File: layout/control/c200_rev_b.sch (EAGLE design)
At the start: 66 parts, among them IC1 STM32F103C8T, IC2 LP2985-SOT23-5, IC3 IC_USBLC6-2, IC4 IC_USBLC6-2, IC5 LT1619ES8, IC6 LP2985-SOT23-5, IC7 IRF7470, T1 LPISR, X1 MINI-USB-SCHIELD-32005-201, Y1 532-CRYSTAL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

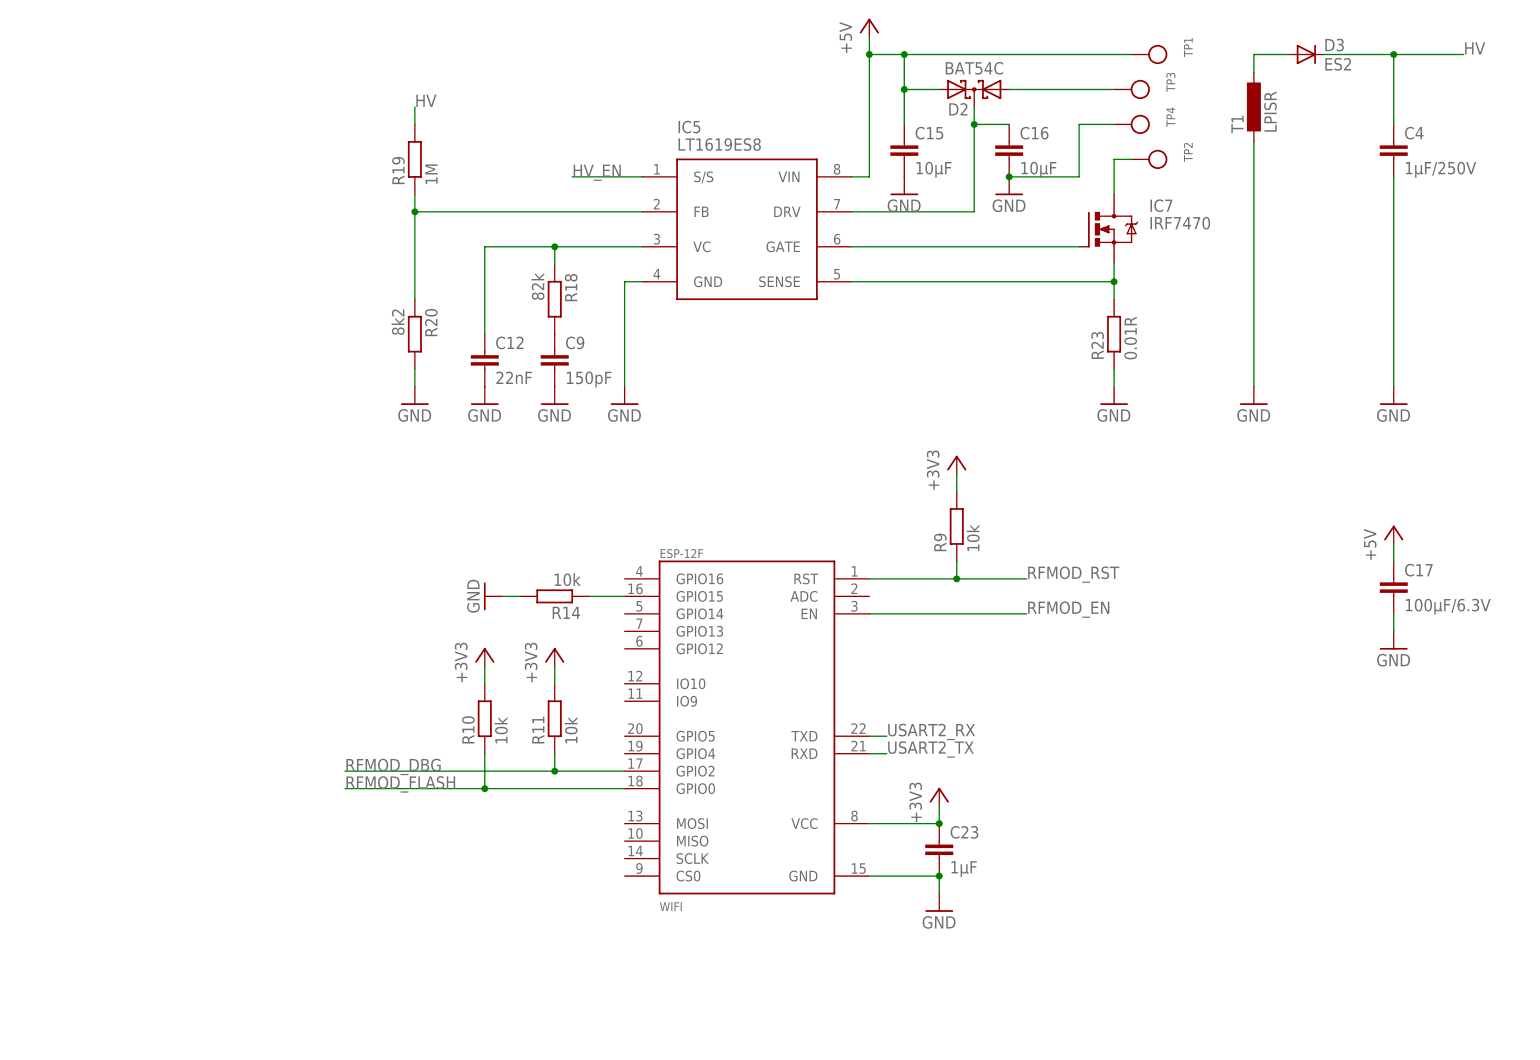
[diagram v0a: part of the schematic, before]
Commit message: Added rev. B of large clock layouts
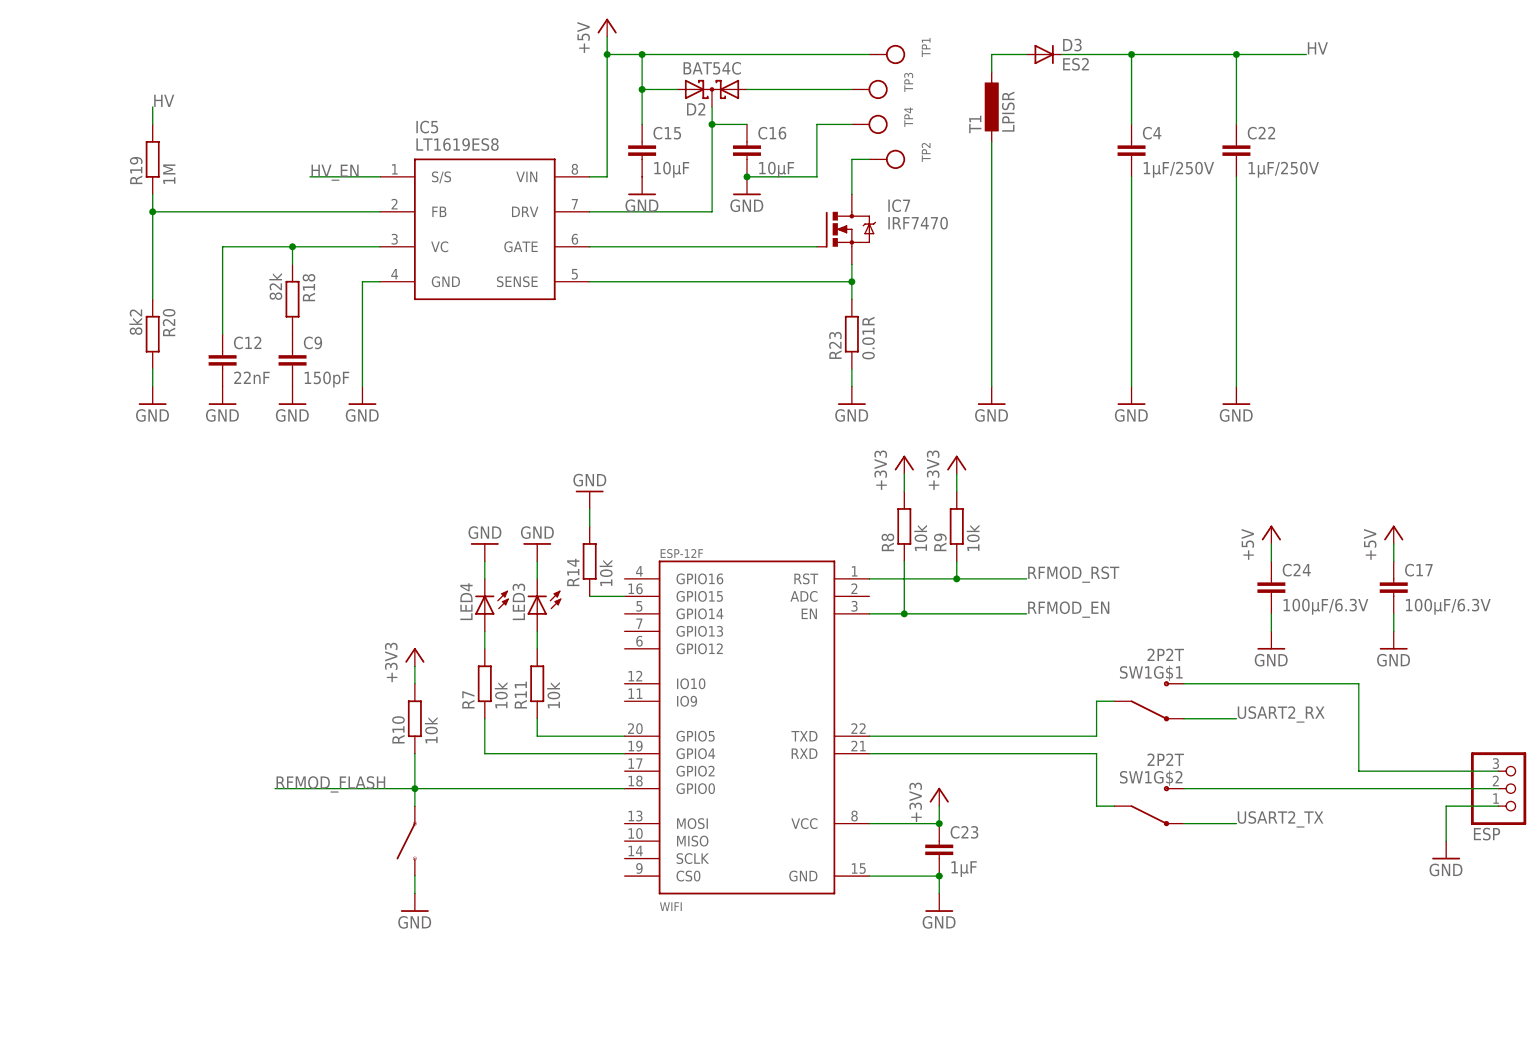
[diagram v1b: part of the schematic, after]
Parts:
- added C22: 1µF/250V, rcl:C-EUC2220K
- added C24: 100µF/6.3V, rcl:C-EUC1210
- added ESP: (no value), microbuilder:HEADER-1X3ROUND
- added FLASH: TACT-SWITCH-40-40, tactile-switch:TACT-SWITCH-40-40
- added LED3, LED4: (no value), led:LEDCHIP-LED0603
- added R7, R8: 10k, rcl:R-EU_R0603
- added SW1: 2P2T, switch:2P2T
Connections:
- new net N$21: SW1G$1.C, WIFI.TXD
- new net N$26: SW1G$2.C, WIFI.RXD
- new net N$27: R11.1, WIFI.GPIO5
- new net N$31: ESP.3, SW1G$1.B
- new net N$32: ESP.2, SW1G$2.B
- new net N$33: R7.1, WIFI.GPIO4
- new net N$34: LED4.A, R7.2
- new net N$35: LED3.A, R11.2
- net +3V3: now also R8.2; no longer R11.2
- net +5V: now also C24.1
- net GND: now also C22.2, C24.2, ESP.1, FLASH.P$1, LED3.C, LED4.C
- net HV: now also C22.1
- net RFMOD_DBG: no longer R11.1, WIFI.GPIO2
- net RFMOD_EN: now also R8.1
- net RFMOD_FLASH: now also FLASH.P$2
- net USART2_RX: now also SW1G$1.A; no longer WIFI.TXD
- net USART2_TX: now also SW1G$2.A; no longer WIFI.RXD
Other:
- moved on the sheet: C12, C15, C16, C4, C9, D2, D3, IC5, IC7, R10, R11, R14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

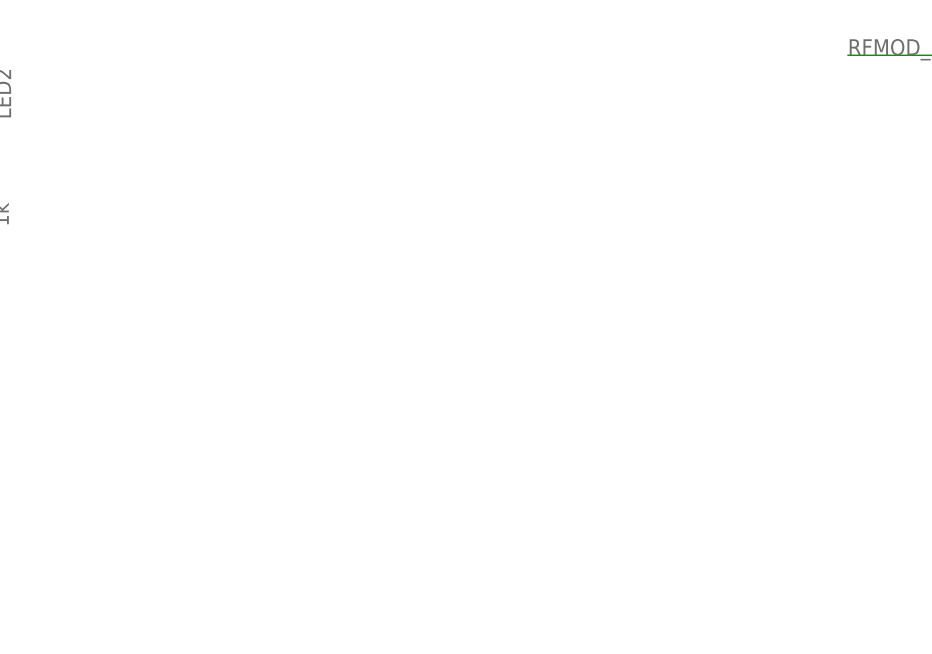
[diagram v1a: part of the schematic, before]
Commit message: Added HV module
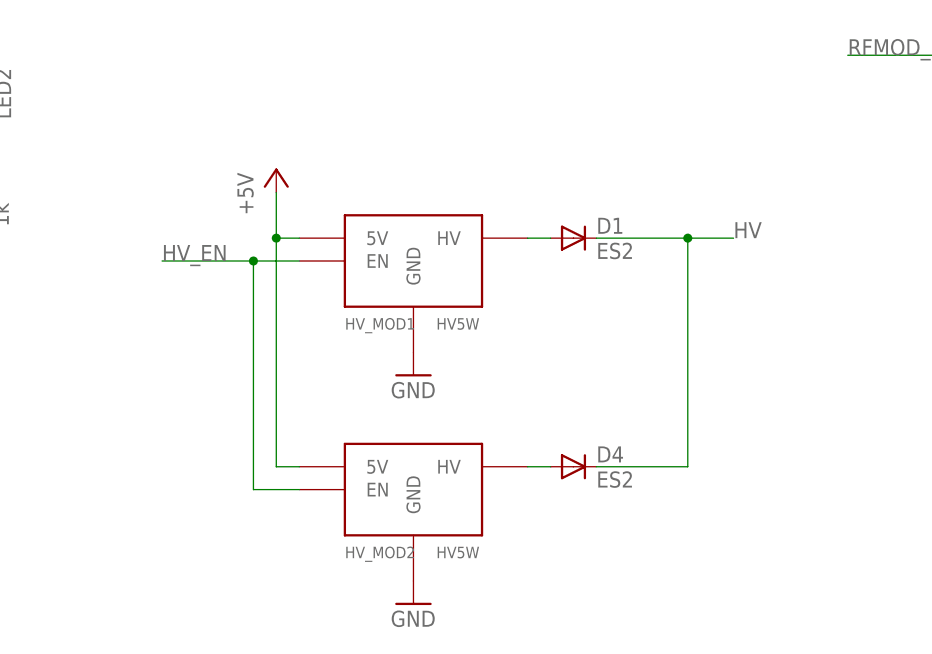
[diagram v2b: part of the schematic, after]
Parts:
- added D1, D4: ES2, diode:ES2
- added HV_MOD1, HV_MOD2: HV5W, hv-mod:HV5W
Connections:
- new net N$40: D1.A, HV_MOD1.HV
- new net N$41: D4.A, HV_MOD2.HV
- net +5V: now also HV_MOD1.5V, HV_MOD2.5V
- net GND: now also HV_MOD1.GND, HV_MOD2.GND
- net HV: now also D1.C, D4.C
- net HV_EN: now also HV_MOD1.EN, HV_MOD2.EN
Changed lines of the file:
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@@
 <?xml version="1.0" encoding="utf-8"?>
 <!DOCTYPE eagle SYSTEM "eagle.dtd">
-<eagle version="6.1">
+<eagle version="7.6.0">
 <drawing>
 <settings>
@@
 <part name="P+8" library="supply1" deviceset="+5V" device=""/>
 <part name="GND42" library="supply1" deviceset="GND" device=""/>
+<part name="HV_MOD1" library="hv-mod" deviceset="HV5W" device=""/>
+<part name="HV_MOD2" library="hv-mod" deviceset="HV5W" device=""/>
+<part name="GND43" library="supply1" deviceset="GND" device=""/>
+<part name="GND44" library="supply1" deviceset="GND" device=""/>
+<part name="D1" library="diode" deviceset="ES2" device=""/>
+<part name="D4" library="diode" deviceset="ES2" device=""/>
+<part name="P+9" library="supply1" deviceset="+5V" device=""/>
 </parts>
 <sheets>
@@
 <instance part="P+8" gate="1" x="497.84" y="104.14"/>
 <instance part="GND42" gate="1" x="497.84" y="86.36"/>
+<instance part="HV_MOD1" gate="G$1" x="304.8" y="43.18"/>
+<instance part="HV_MOD2" gate="G$1" x="304.8" y="17.78"/>
+<instance part="GND43" gate="1" x="304.8" y="5.08"/>
+<instance part="GND44" gate="1" x="304.8" y="30.48"/>
+<instance part="D1" gate="G$1" x="322.58" y="45.72"/>
+<instance part="D4" gate="G$1" x="322.58" y="20.32"/>
+<instance part="P+9" gate="1" x="289.56" y="53.34"/>
 </instances>
 <busses>
@@
 <wire x1="497.84" y1="91.44" x2="497.84" y2="88.9" width="0.1524" layer="91"/>
 </segment>
+<segment>
+<pinref part="HV_MOD2" gate="G$1" pin="GND"/>
+<pinref part="GND43" gate="1" pin="GND"/>
+</segment>
+<segment>
+<pinref part="HV_MOD1" gate="G$1" pin="GND"/>
+<pinref part="GND44" gate="1" pin="GND"/>
+</segment>
 </net>
 <net name="+5V" class="0">
@@
 <pinref part="C24" gate="G$1" pin="1"/>
 <wire x1="497.84" y1="101.6" x2="497.84" y2="99.06" width="0.1524" layer="91"/>
+</segment>
+<segment>
+<pinref part="HV_MOD2" gate="G$1" pin="5V"/>
+<wire x1="292.1" y1="20.32" x2="289.56" y2="20.32" width="0.1524" layer="91"/>
+<wire x1="289.56" y1="20.32" x2="289.56" y2="45.72" width="0.1524" layer="91"/>
+<pinref part="HV_MOD1" gate="G$1" pin="5V"/>
+<wire x1="289.56" y1="45.72" x2="292.1" y2="45.72" width="0.1524" layer="91"/>
+<junction x="289.56" y="45.72"/>
+<wire x1="289.56" y1="45.72" x2="289.56" y2="50.8" width="0.1524" layer="91"/>
+<pinref part="P+9" gate="1" pin="+5V"/>
 </segment>
 </net>
@@
 <label x="241.3" y="127" size="1.778" layer="95"/>
 </segment>
+<segment>
+<pinref part="HV_MOD1" gate="G$1" pin="EN"/>
+<wire x1="292.1" y1="43.18" x2="287.02" y2="43.18" width="0.1524" layer="91"/>
+<wire x1="287.02" y1="43.18" x2="287.02" y2="17.78" width="0.1524" layer="91"/>
+<pinref part="HV_MOD2" gate="G$1" pin="EN"/>
+<wire x1="287.02" y1="17.78" x2="292.1" y2="17.78" width="0.1524" layer="91"/>
+<wire x1="287.02" y1="43.18" x2="276.86" y2="43.18" width="0.1524" layer="91"/>
+<junction x="287.02" y="43.18"/>
+<label x="276.86" y="43.18" size="1.778" layer="95"/>
+</segment>
 </net>
 <net name="N$20" class="0">
@@
 <wire x1="106.68" y1="86.36" x2="114.3" y2="86.36" width="0.1524" layer="91"/>
 </segment>
+<segment>
+<pinref part="D4" gate="G$1" pin="C"/>
+<wire x1="325.12" y1="20.32" x2="335.28" y2="20.32" width="0.1524" layer="91"/>
+<wire x1="335.28" y1="20.32" x2="335.28" y2="45.72" width="0.1524" layer="91"/>
+<pinref part="D1" gate="G$1" pin="C"/>
+<wire x1="335.28" y1="45.72" x2="325.12" y2="45.72" width="0.1524" layer="91"/>
+<wire x1="335.28" y1="45.72" x2="340.36" y2="45.72" width="0.1524" layer="91"/>
+<junction x="335.28" y="45.72"/>
+<label x="340.36" y="45.72" size="1.778" layer="95"/>
+</segment>
 </net>
 <net name="NX_EN" class="0">
@@
 </segment>
 </net>
+<net name="N$40" class="0">
+<segment>
+<pinref part="HV_MOD1" gate="G$1" pin="HV"/>
+<pinref part="D1" gate="G$1" pin="A"/>
+<wire x1="317.5" y1="45.72" x2="320.04" y2="45.72" width="0.1524" layer="91"/>
+</segment>
+</net>
+<net name="N$41" class="0">
+<segment>
+<pinref part="HV_MOD2" gate="G$1" pin="HV"/>
+<pinref part="D4" gate="G$1" pin="A"/>
+<wire x1="317.5" y1="20.32" x2="320.04" y2="20.32" width="0.1524" layer="91"/>
+</segment>
+</net>
